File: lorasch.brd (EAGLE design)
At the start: 130 x 53 mm, 12 parts, among them M1 ARDUINO-NANO-3.0

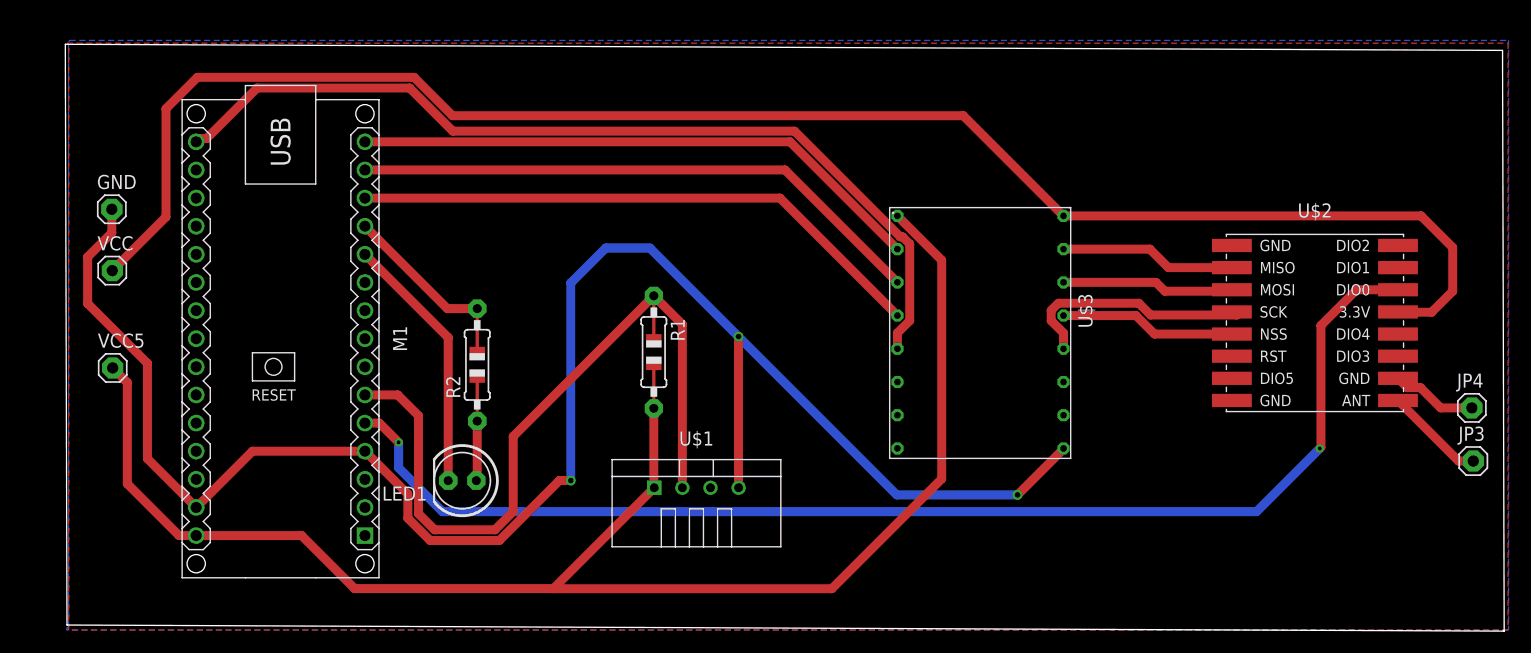
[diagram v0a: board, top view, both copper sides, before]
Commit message: Modify schematic to reduce size of board.
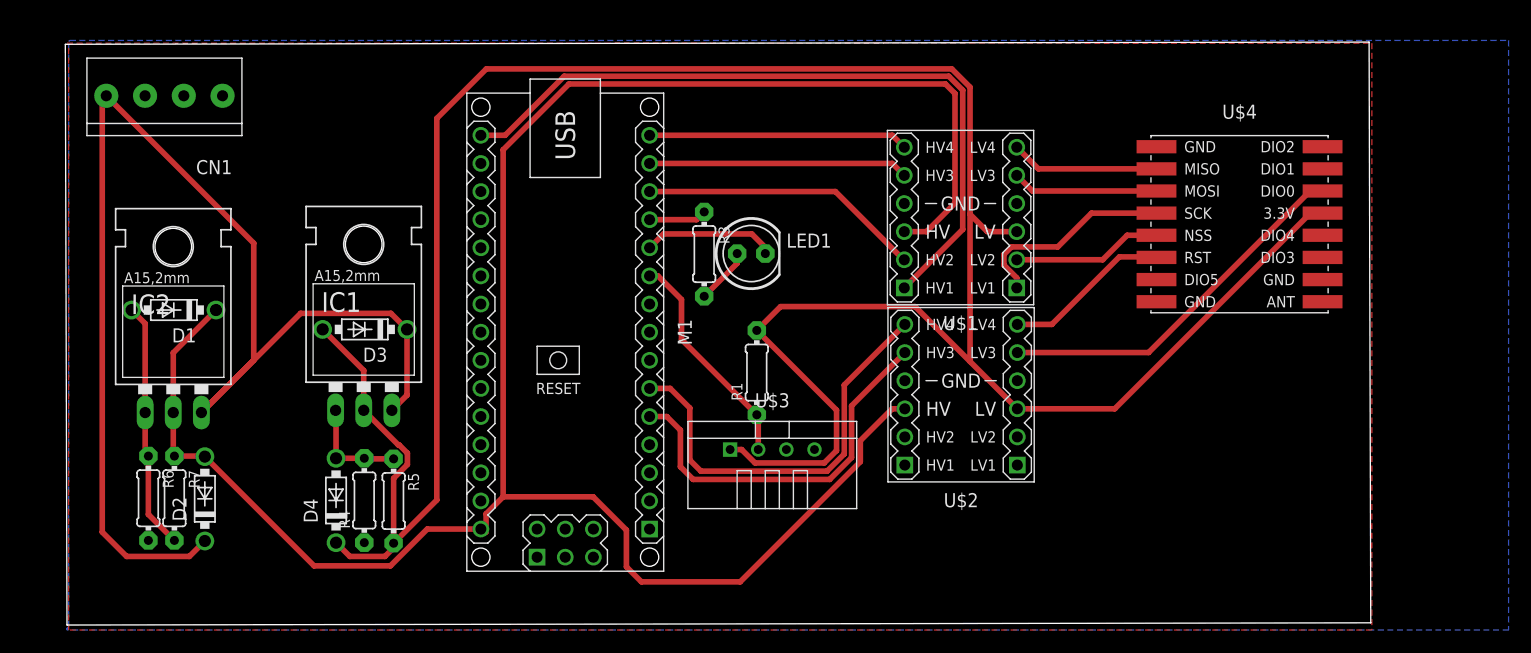
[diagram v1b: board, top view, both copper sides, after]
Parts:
- removed GND, JP3, JP4, VCC, VCC5: (no value), adafruit:1X01
- removed R2: (no value), adafruit:0805-THM
- added CN1: 1X4-3.5MM, adafruit:1X04-3.5MM
- added D1, D2, D3, D4: 1N5817-B, diode:DO41-7.6
- added IC1: 3v3, v-reg:317TL
- added IC2: 5v, v-reg:317TL
- added R3: 220, adafruit:0204/7
- added R4: 2.7k, adafruit:0204/7
- added R5: 4.7k, adafruit:0204/7
- added R6: 1.5k, adafruit:0204/7
- added R7: (no value), adafruit:0204/7
- added U$4: WIRELESS-LORA-RFM95W#SMD, dht22:WIRELESS-LORA-RFM95W#SMD
- M1: value ARDUINO-NANO-3.0 -> ARDUINO-NANO-3.0#ISP; device dht22:ARDUINO-NANO-3.0 -> dht22:ARDUINO-NANO-3.0#ISP
- R1: value (none) -> 10k; device adafruit:0805-THM -> adafruit:0204/7
- U$1: value TEMP-HUM-SENSOR-DHT22 -> LEVEL-SHIFTER-4CH; device dht22:TEMP-HUM-SENSOR-DHT22 -> dht22:LEVEL-SHIFTER-4CH
- U$2: value WIRELESS-LORA-RFM95W#SMD -> LEVEL-SHIFTER-4CH; device dht22:WIRELESS-LORA-RFM95W#SMD -> dht22:LEVEL-SHIFTER-4CH
- U$3: value (none) -> TEMP-HUM-SENSOR-DHT22; device logicconv:TX50108E -> dht22:TEMP-HUM-SENSOR-DHT22
- moved U$1 34.1 mm to (80.7, 36.8), turned to 180 degrees
- moved LED1 33.2 mm to (61.8, 33.5), turned to 0 degrees
- moved U$2 32.6 mm to (80.8, 20.8), turned to 180 degrees
- moved M1 25.7 mm to (45.0, 26.4)
- moved U$3 21.6 mm to (63.7, 15.8), turned to 0 degrees
- moved R1 9.48 mm to (62.3, 22.8), turned to 90 degrees
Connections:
- net N$8 renamed LEDGND
- removed net 3V3: M1.J2.14
- removed net 5V: M1.J2.4
- removed net DATA: M1.J1.6, R1.1, U$1.2
- removed net DIO0: M1.J1.5, U$2.B3
- removed net N$10: U$2.A5, U$3.13
- removed net N$11: U$2.A4, U$3.12
- removed net N$12: U$2.A3, U$3.14
- removed net VCC: U$2.B4, U$3.16, VCC.1
- removed net VCC5: M1.J2.1, R1.2, U$1.1, U$3.1, VCC5.1
- new net 3V3.1: D3.A, D4.C, IC1.2, M1.J2.14, R1.2, R5.2, U$1.J1.3, U$2.J1.3, U$3.1, U$4.B4
- new net 5.1V: D1.C, D2.A, IC2.2, M1.J2.1, M1.J2.4, R7.1, U$1.J2.3, U$2.J2.3
- new net 9V: CN1.1, D2.C, D3.C, IC1.3, IC2.3
- new net D7: M1.J1.10, R1.1, U$3.2
- new net INT: U$2.J1.5, U$4.B3
- new net LED+: M1.J1.12, R3.1
- new net N$14: U$1.J1.5, U$4.A3
- new net N$15: U$1.J1.2, U$4.A5
- new net N$16: U$1.J1.1, U$4.A4
- new net N$17: U$2.J1.6, U$4.A6
- new net N$5: D1.A, IC2.1, R6.1, R7.2
- new net N$8: M1.J1.14, U$1.J2.5
- net GND: now also CN1.2, R4.1, R6.2, U$1.J1.4, U$1.J2.4, U$2.J1.4, U$2.J2.4, U$3.4, U$4.A1, U$4.A8, U$4.B7; no longer GND.1, JP4.1, U$1.4, U$2.A1, U$2.A8, U$2.B7, U$3.9
- net N$1: now also D4.A, IC1.1, R4.2, R5.1; no longer M1.J1.15, U$3.2
- net N$13: now also U$1.J1.6, U$4.A2; no longer U$2.A2, U$3.15
- net N$2: now also LED1.A, R3.2; no longer M1.J1.14, U$3.3
- net N$3: now also M1.J2.15, U$1.J2.1; no longer M1.J1.13, U$3.4
- net N$4: now also M1.J1.5, U$2.J2.5; no longer M1.J2.15, U$3.5
- net N$6: now also M1.J1.6, U$2.J2.6; no longer M1.J1.12, R2.2
- net N$7: now also M1.J1.15, U$1.J2.6; no longer LED1.A, R2.1
- net N$9: now also M1.J1.13, U$1.J2.2; no longer JP3.1, U$2.B8
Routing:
- net 3V3.1: track 0.00 -> 237.4 mm
- net 5.1V: track 0.00 -> 192.5 mm
- net GND: track 170.8 -> 0.00 mm, vias 3 -> 0
- net VCC: track 150.1 -> 0.00 mm
- net VCC5: track 138.2 -> 0.00 mm
- net 9V: track 0.00 -> 117.2 mm
- net DIO0: track 112.7 -> 0.00 mm, vias 2 -> 0
- net DATA: track 67.4 -> 0.00 mm
- net N$4: track 82.2 -> 34.8 mm
- net N$2: track 52.3 -> 5.09 mm
- net N$1: track 52.1 -> 9.57 mm
- net INT: track 0.00 -> 33.6 mm
- net N$6: track 13.2 -> 38.0 mm
- net N$8: track 0.00 -> 23.4 mm
- net N$5: track 0.00 -> 22.4 mm
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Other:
- board size 130 x 53 mm -> 117.9 x 52.6 mm

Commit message: Connect all grounds to common plane.
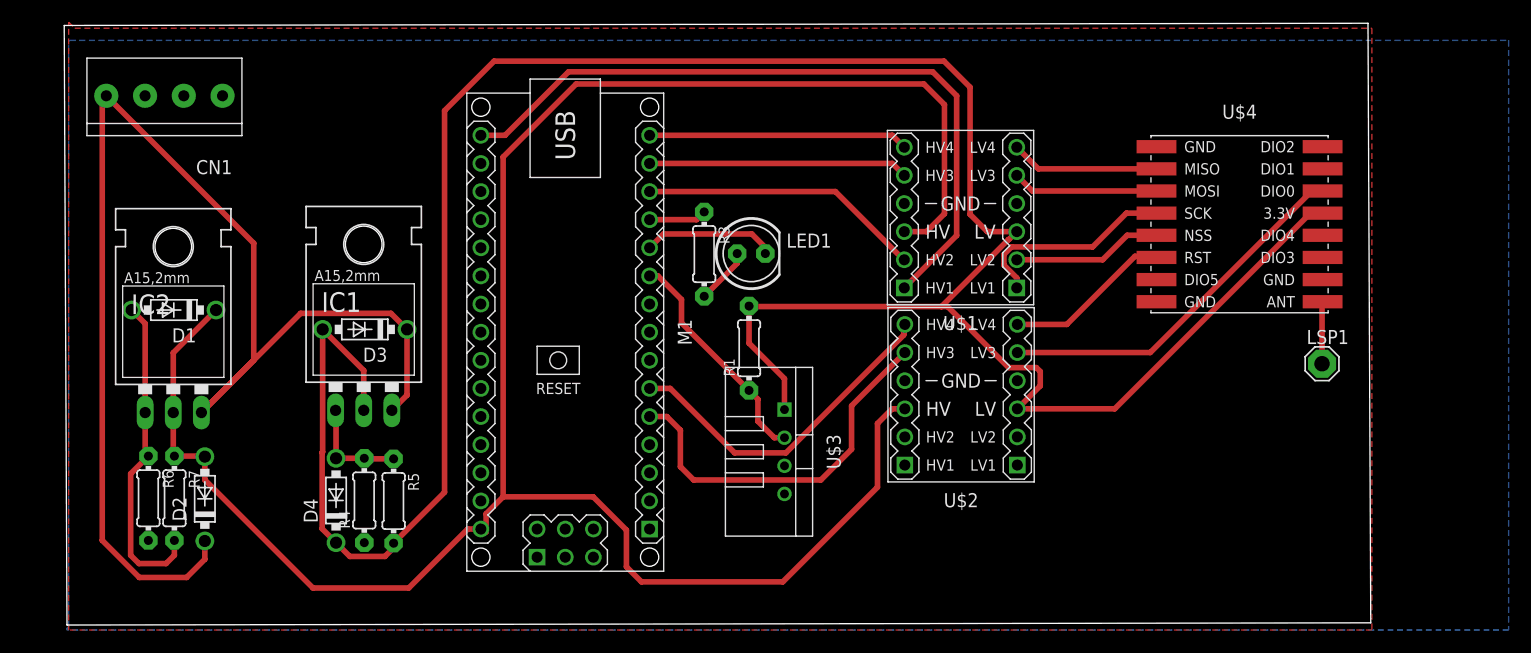
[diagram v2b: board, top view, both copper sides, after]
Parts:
- added LSP1: SE14, solpad:SE14
- moved R1 2.31 mm to (61.6, 25.0)
- moved U$3 1.12 mm to (64.8, 15.7), turned to 270 degrees
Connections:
- new net N$10: LSP1.MP, U$4.B8
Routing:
- net N$6: track 38.0 -> 30.8 mm
- net N$5: track 22.4 -> 29.3 mm
- net 3V3.1: track 237.4 -> 230.9 mm
- net N$10: track 0.00 -> 5.62 mm
- net 9V: track 117.2 -> 120.1 mm
- net 5.1V: track 192.5 -> 195.4 mm
- net D7: track 20.2 -> 21.0 mm
- net N$3: track 66.3 -> 65.6 mm
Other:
- board size 117.9 x 52.6 mm -> 118 x 54.4 mm

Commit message: Change size of board.
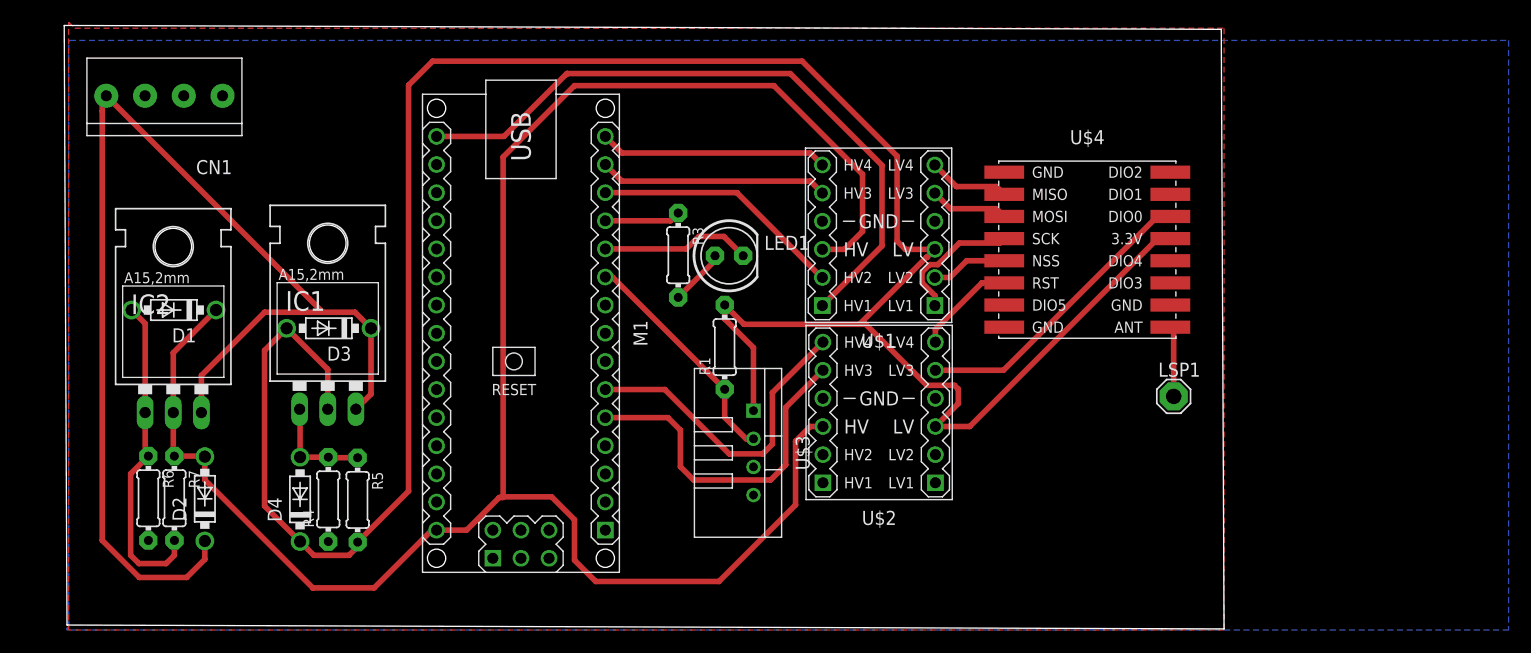
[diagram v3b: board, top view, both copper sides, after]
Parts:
- moved U$4 13.9 mm to (92.2, 33.9)
- moved LSP1 13.7 mm to (100.0, 20.6)
- moved U$1 7.57 mm to (73.3, 35.2)
- moved U$2 7.57 mm to (73.3, 19.2)
- moved M1 4.00 mm to (41.0, 26.4)
- moved D3 3.25 mm to (23.6, 26.8)
- moved D4 3.25 mm to (21.1, 11.3)
- moved IC1 3.25 mm to (23.6, 23.3)
- moved R4 3.25 mm to (23.6, 11.3)
- moved R5 3.25 mm to (26.2, 11.3)
- moved U$3 2.80 mm to (62.0, 15.6)
- moved R3 2.35 mm to (55.2, 33.4)
- moved R1 2.20 mm to (59.4, 25.1)
- moved LED1 2.01 mm to (59.8, 33.4)
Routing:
- net 5.1V: track 195.4 -> 176.2 mm
- net 3V3.1: track 230.9 -> 216.8 mm
- net 9V: track 120.1 -> 110.5 mm
- net N$17: track 16.5 -> 9.11 mm
- net INT: track 33.6 -> 27.0 mm
- net N$15: track 13.5 -> 6.90 mm
- net N$16: track 18.8 -> 12.2 mm
- net N$14: track 13.2 -> 7.14 mm
- net N$13: track 13.4 -> 7.37 mm
- net N$3: track 65.6 -> 61.0 mm
- net N$4: track 34.4 -> 31.1 mm
- net N$9: track 25.6 -> 22.8 mm
- net N$8: track 23.4 -> 20.7 mm
- net N$7: track 23.4 -> 20.7 mm
- net N$6: track 30.8 -> 29.0 mm
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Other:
- board size 118 x 54.4 mm -> 104.8 x 54.5 mm

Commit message: Add arduino pro mini 5v.
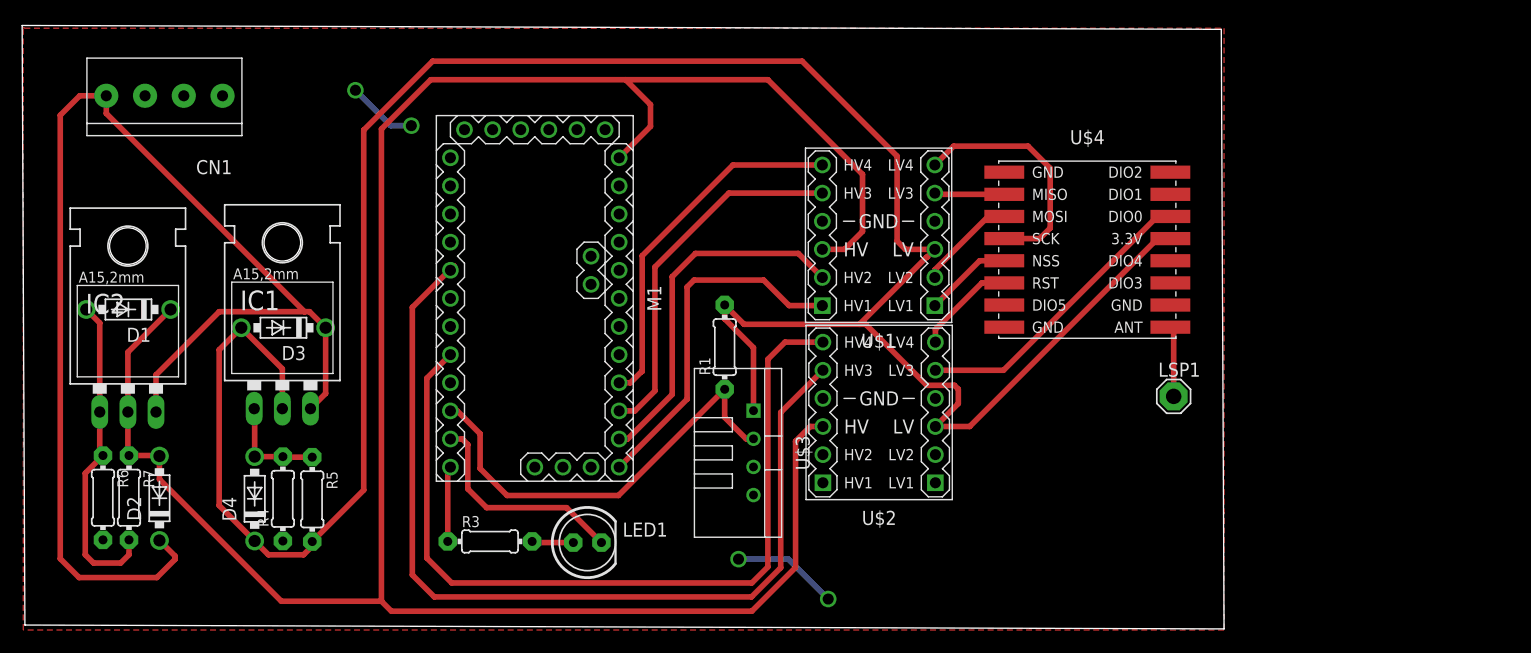
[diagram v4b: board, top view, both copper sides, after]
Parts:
- M1: value ARDUINO-NANO-3.0#ISP -> ARDUINO-PRO-MINI-5.0V; device dht22:ARDUINO-NANO-3.0#ISP -> dht22:ARDUINO-PRO-MINI
- moved R3 30.9 mm to (38.2, 7.55), turned to 0 degrees
- moved LED1 28.9 mm to (47.0, 7.45)
- moved D4 4.10 mm to (16.9, 11.4)
- moved IC1 4.10 mm to (19.4, 23.4)
- moved R4 4.10 mm to (19.5, 11.4)
- moved R5 4.10 mm to (22.1, 11.3)
- moved D1 4.10 mm to (5.55, 28.5)
- moved D2 4.10 mm to (8.35, 11.4)
- moved IC2 4.10 mm to (5.50, 23.1)
- moved R6 4.10 mm to (3.25, 11.5)
- moved R7 4.10 mm to (5.60, 11.5)
- moved D3 4.10 mm to (19.6, 26.9)
- moved M1 3.39 mm to (42.2, 29.5)
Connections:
- removed net N$16: U$1.J1.1, U$4.A4
- removed net N$6: M1.J1.6, U$2.J2.6
- new net N$11: U$1.J1.2, U$4.A3
- new net N$12: U$1.J1.5, U$4.A2
- new net VCC: M1.J6.4
- net 3V3.1: no longer M1.J2.14
- net 5.1V: now also M1.J6.1; no longer M1.J2.1, M1.J2.4
- net D7: now also M1.J7.3; no longer M1.J1.10
- net GND: now also M1.J6.2, M1.J7.9; no longer M1.J1.4, M1.J2.2
- net LED+: now also M1.J7.1; no longer M1.J1.12
- net LEDGND: now also M1.J7.2; no longer M1.J1.11
- net N$13: now also U$4.A4; no longer U$4.A2
- net N$14: now also M1.J6.9, U$1.J2.6; no longer U$1.J1.5, U$4.A3
- net N$15: now also U$1.J1.1; no longer U$1.J1.2
- net N$3: now also M1.J6.10, U$1.J2.5; no longer M1.J2.15, U$1.J2.1
- net N$4: now also M1.J6.11, U$1.J2.2; no longer M1.J1.5, U$2.J2.5
- net N$7: now also M1.J6.12, U$1.J2.1; no longer M1.J1.15, U$1.J2.6
- net N$8: now also M1.J7.5, U$2.J2.6; no longer M1.J1.14, U$1.J2.5
- net N$9: now also M1.J7.8, U$2.J2.5; no longer M1.J1.13, U$1.J2.2
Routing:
- net N$9: track 22.8 -> 84.6 mm
- net N$8: track 20.7 -> 75.9 mm
- net 5.1V: track 176.2 -> 208.2 mm
- net N$6: track 29.0 -> 0.00 mm
- net N$3: track 61.0 -> 33.0 mm
- net N$14: track 7.14 -> 32.6 mm
- net D7: track 21.3 -> 40.0 mm
- net GND: track 0.00 -> 16.0 mm, vias 0 -> 4
- net N$13: track 7.37 -> 21.9 mm
- net N$16: track 12.2 -> 0.00 mm
- net N$7: track 20.7 -> 32.2 mm
- net N$11: track 0.00 -> 8.96 mm
- net N$12: track 0.00 -> 6.32 mm
- net LEDGND: track 13.6 -> 19.9 mm
- net 9V: track 110.5 -> 115.4 mm
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- removed copper zone on layer 16, net GND
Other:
- board size 104.8 x 54.5 mm -> 108.5 x 54.5 mm
